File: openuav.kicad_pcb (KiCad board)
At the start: 4 copper layers, 36 x 36 mm, 72 parts, among them J1 Conn_01x01, J10 Conn_01x01, J11 Conn_01x01, J12 Conn_01x01, J13 Conn_01x01, J14 Conn_01x01, J15 Conn_01x01, J16 Conn_01x01, J17 Conn_ARM_SWD_TagConnect_TC203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, J19 Conn_01x01, J2 Conn_01x01, J20 Conn_01x01, J21 Conn_01x01, J22 Conn_01x01, J23 Conn_01x01, J24 Conn_01x01, J25 Conn_01x01, J26 Conn_01x01, J27 Conn_01x01, J28 Conn_01x01, J29 Conn_01x01, J3 Conn_01x01, J30 Conn_01x01, J31 Conn_01x01, J4 Conn_01x01, J5 Conn_01x01, J6 Conn_01x01, J7 Conn_01x01, J8 Conn_01x01, J9 Conn_01x01, J99 USB_C_Receptacle_USB2.0, Q2 AO3400A, SW1 SW_Push, U1 STM32G474CETx, U2 BMI270, U3 BMP280, U5 TPS54202DDC, U6 W25N01GVZEIG, U7 XC6206P332MR

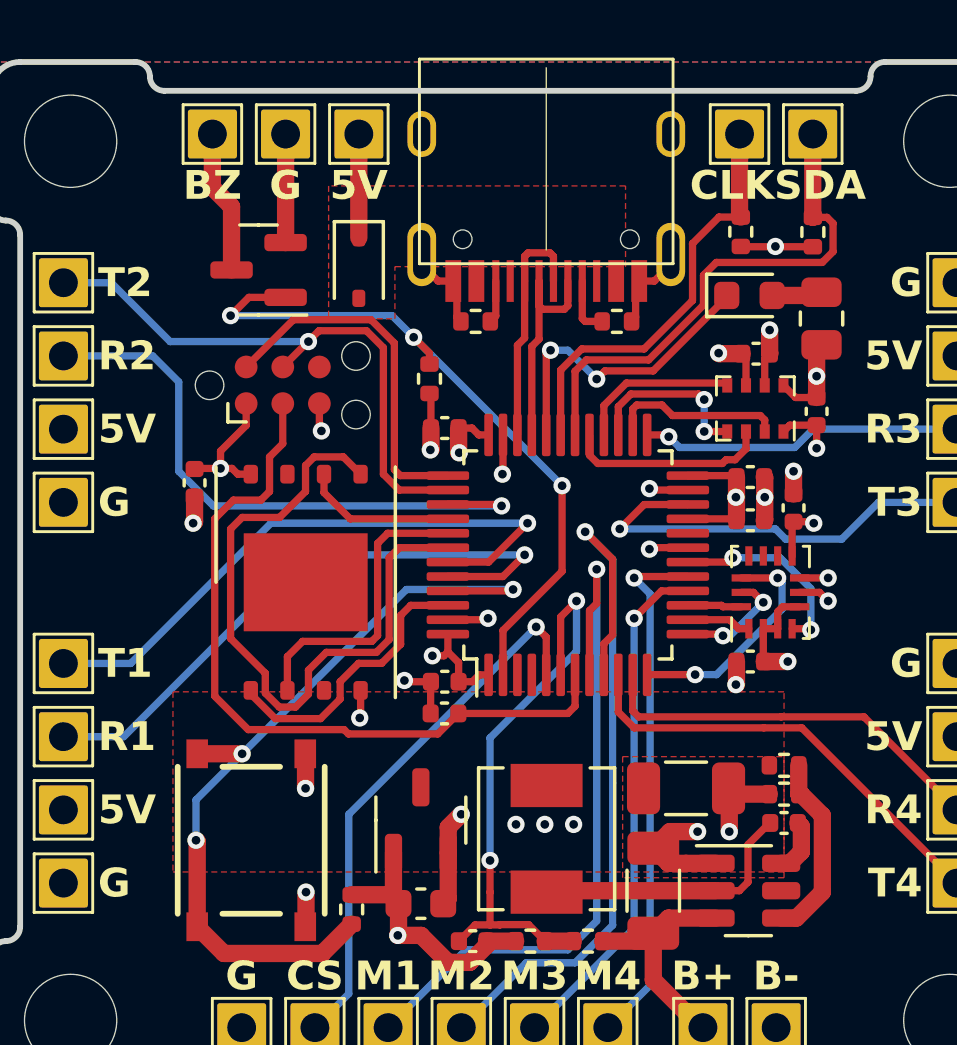
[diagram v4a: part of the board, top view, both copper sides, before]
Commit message: rearrange buzzer pins to keep +5v away from USB GND
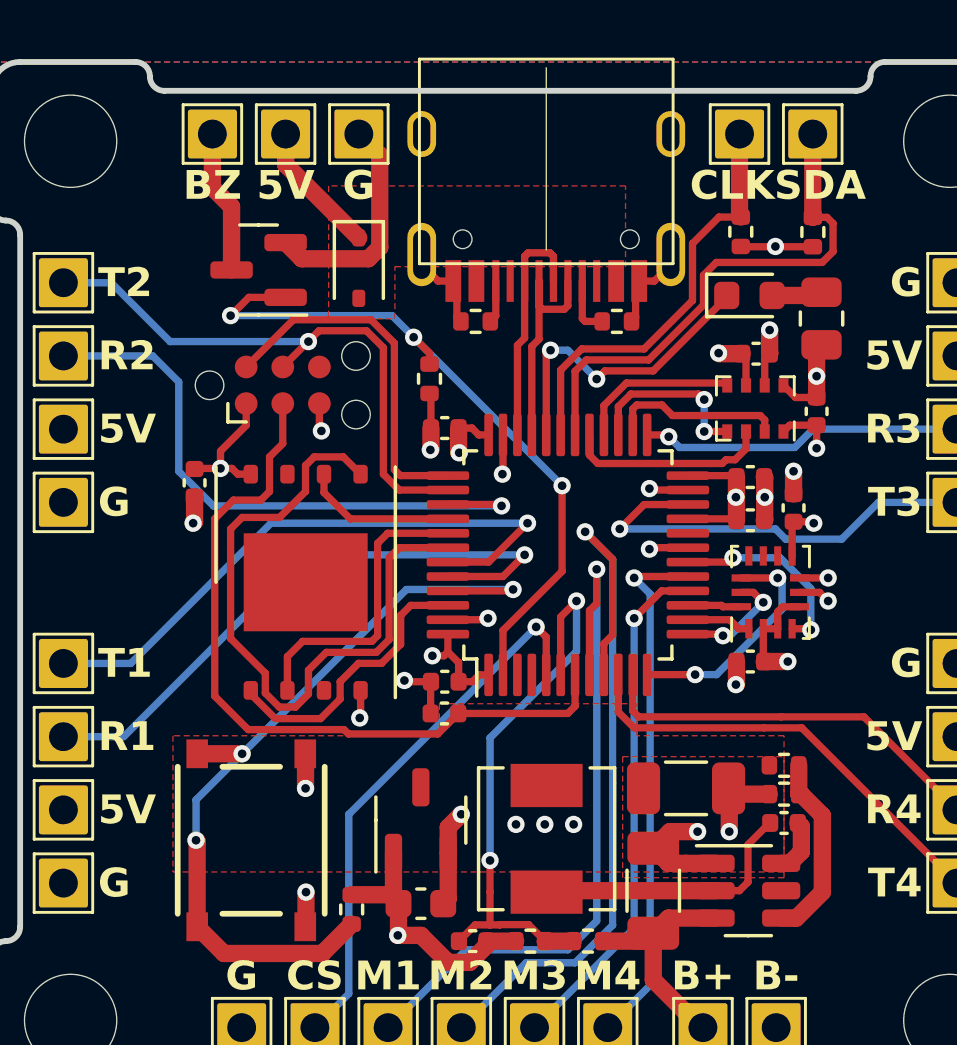
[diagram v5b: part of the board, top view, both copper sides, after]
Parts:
- moved J27 2.54 mm to (142.7, 52.5)
- moved J28 2.54 mm to (140.2, 52.5)
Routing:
- net GND: track 48.1 -> 52.3 mm
- net +5V: track 3.60 -> 4.65 mm
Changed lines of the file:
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@@
   )
   (footprint "Connector_Custom_Pads:TP-2.54" (layer "F.Cu")
-    (at 142.748 52.5 180)
+    (at 140.208 52.5 180)
     (property "Sheetfile" "openuav.kicad_sch")
     (property "Sheetname" "")
@@
   )
   (footprint "Connector_Custom_Pads:TP-2.54" (layer "F.Cu")
-    (at 140.208 52.5 180)
+    (at 142.748 52.5 180)
     (property "Sheetfile" "openuav.kicad_sch")
     (property "Sheetname" "")
@@
     (effects (font (size 1.5 1.5) (thickness 0.3) bold) (justify left bottom mirror))
   )
-  (gr_text "G" (at 140.208 53.7) (layer "F.SilkS")
+  (gr_text "G" (at 142.748 53.7) (layer "F.SilkS")
     (effects (font (size 1 1) (thickness 0.2) bold) (justify top))
   )
@@
     (effects (font (size 1 1) (thickness 0.2) bold) (justify bottom))
   )
-  (gr_text "5V" (at 142.748 53.7) (layer "F.SilkS")
+  (gr_text "5V" (at 140.208 53.7) (layer "F.SilkS")
     (effects (font (size 1 1) (thickness 0.2) bold) (justify top))
   )
@@
   (segment (start 146.594859 81.237) (end 147.18 80.651859) (width 0.6) (layer "F.Cu") (net 2))
   (segment (start 157 59.3) (end 157 60.11) (width 0.6) (layer "F.Cu") (net 2))
+  (segment (start 143.475 56.435968) (end 143.475 53.227) (width 0.6) (layer "F.Cu") (net 2))
   (segment (start 156.83 65.88) (end 156.81 65.9) (width 0.6) (layer "F.Cu") (net 2))
   (segment (start 152.35 57.6) (end 152.35 58.86) (width 0.254) (layer "F.Cu") (net 2))
   (segment (start 145.845142 81.237) (end 146.594859 81.237) (width 0.6) (layer "F.Cu") (net 2))
+  (segment (start 143.475 53.227) (end 142.748 52.5) (width 0.6) (layer "F.Cu") (net 2))
   (segment (start 144.93 57.03) (end 145.5 57.6) (width 0.254) (layer "F.Cu") (net 2))
   (segment (start 145.24 71.51) (end 145.25 71.5) (width 0.254) (layer "F.Cu") (net 2))
@@
   (segment (start 154.5 76.7) (end 153.5375 76.7) (width 0.6) (layer "F.Cu") (net 2))
   (segment (start 137.05 65.08) (end 137.05 65.95) (width 0.6) (layer "F.Cu") (net 2))
-  (segment (start 140.208 52.5) (end 140.208 56.266) (width 0.6) (layer "F.Cu") (net 2))
   (segment (start 146.15 57.6) (end 146.15 58.86) (width 0.254) (layer "F.Cu") (net 2))
   (segment (start 153.5375 76.7) (end 152.9625 77.275) (width 0.6) (layer "F.Cu") (net 2))
   (segment (start 145.24 72.6) (end 145.24 71.51) (width 0.254) (layer "F.Cu") (net 2))
+  (segment (start 143.083968 56.827) (end 143.475 56.435968) (width 0.6) (layer "F.Cu") (net 2))
   (segment (start 152.35 58.86) (end 152.21 59) (width 0.254) (layer "F.Cu") (net 2))
   (segment (start 156.83 64.42) (end 156.81 64.4) (width 0.6) (layer "F.Cu") (net 2))
@@
   (segment (start 154.1625 64.85) (end 152.88 64.85) (width 0.254) (layer "F.Cu") (net 2))
   (segment (start 137.05 65.95) (end 137 66) (width 0.6) (layer "F.Cu") (net 2))
+  (segment (start 140.208 56.266) (end 140.769 56.827) (width 0.6) (layer "F.Cu") (net 2))
   (segment (start 153.57 56.68) (end 153.57 57.03) (width 0.254) (layer "F.Cu") (net 2))
   (segment (start 158.63 62.6) (end 158.63 63.4) (width 0.254) (layer "F.Cu") (net 2))
   (segment (start 144.1 80.3) (end 144.908141 80.3) (width 0.6) (layer "F.Cu") (net 2))
   (segment (start 157 60.11) (end 157.01 60.12) (width 0.6) (layer "F.Cu") (net 2))
+  (segment (start 140.769 56.827) (end 143.083968 56.827) (width 0.6) (layer "F.Cu") (net 2))
   (segment (start 153.57 57.03) (end 153 57.6) (width 0.254) (layer "F.Cu") (net 2))
   (segment (start 158.73 68.4) (end 159.03 68.7) (width 0.254) (layer "F.Cu") (net 2))
@@
   (via (at 158.53 66) (size 0.6) (drill 0.3) (layers "F.Cu" "B.Cu") (net 4))
   (via (at 157.2 56.4) (size 0.6) (drill 0.3) (layers "F.Cu" "B.Cu") (net 4))
-  (segment (start 142.748 52.5) (end 142.748 56.1) (width 0.6) (layer "F.Cu") (net 5))
+  (segment (start 140.208 53.56) (end 142.748 56.1) (width 0.6) (layer "F.Cu") (net 5))
+  (segment (start 140.208 52.5) (end 140.208 53.56) (width 0.6) (layer "F.Cu") (net 5))
   (via (at 150.2 76.45) (size 0.6) (drill 0.3) (layers "F.Cu" "B.Cu") (free) (net 5))
   (via (at 149.2 76.45) (size 0.6) (drill 0.3) (layers "F.Cu" "B.Cu") (free) (net 5))
@@
     (polygon
       (pts
-        (xy 157.5 71.85)
-        (xy 136.3 71.85)
+        (xy 157.5 73.374)
+        (xy 152.4 73.374)
+        (xy 152.4 72.263)
+        (xy 145.542 72.263)
+        (xy 145.542 73.374)
+        (xy 136.3 73.374)
         (xy 136.3 78.1)
         (xy 157.5 78.1)
@@
   (zone (net 0) (net_name "") (layers "F&B.Cu") (hatch edge 0.5)
     (priority 1)
-    (connect_pads (clearance 0.3))
+    (connect_pads (clearance 0.25))
     (min_thickness 0.5) (filled_areas_thickness no)
     (fill yes (thermal_gap 0.5) (thermal_bridge_width 0.5) (island_removal_mode 1) (island_area_min 10))

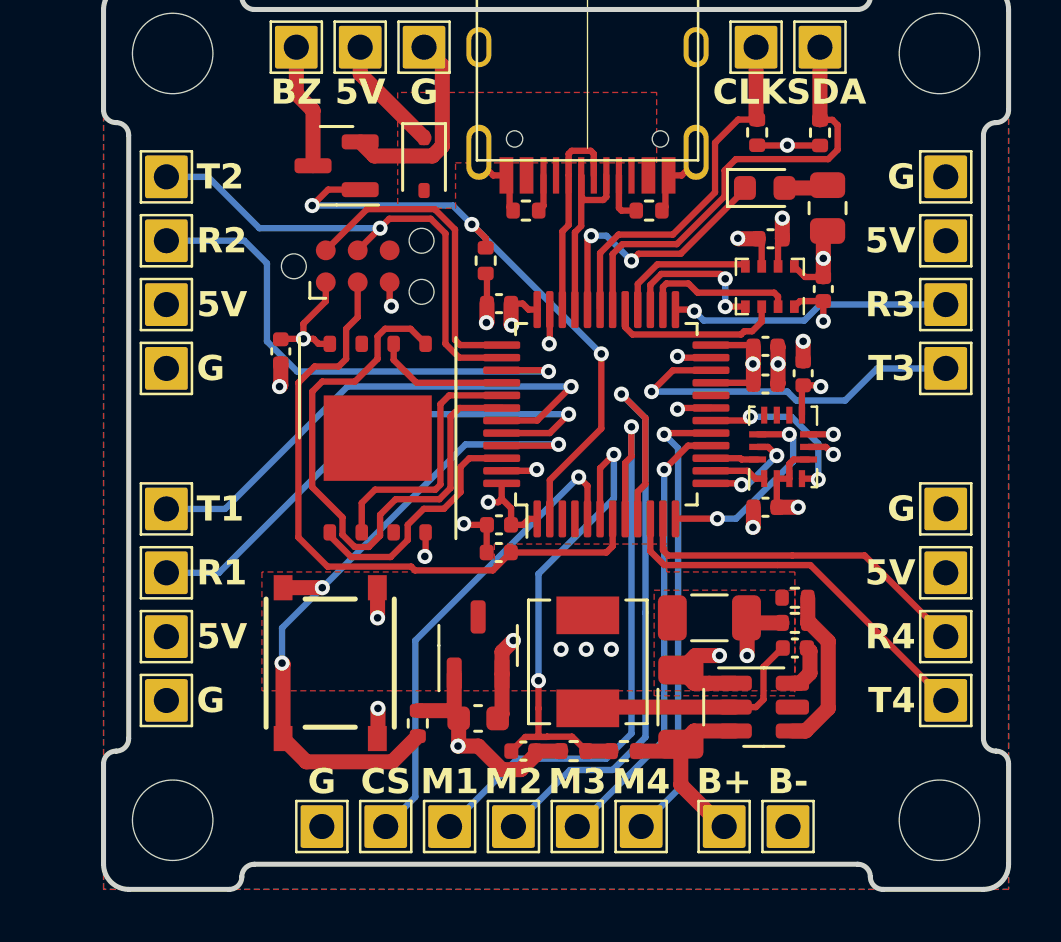
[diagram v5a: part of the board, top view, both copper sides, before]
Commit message: add vtx power switch, use smaller dfu button
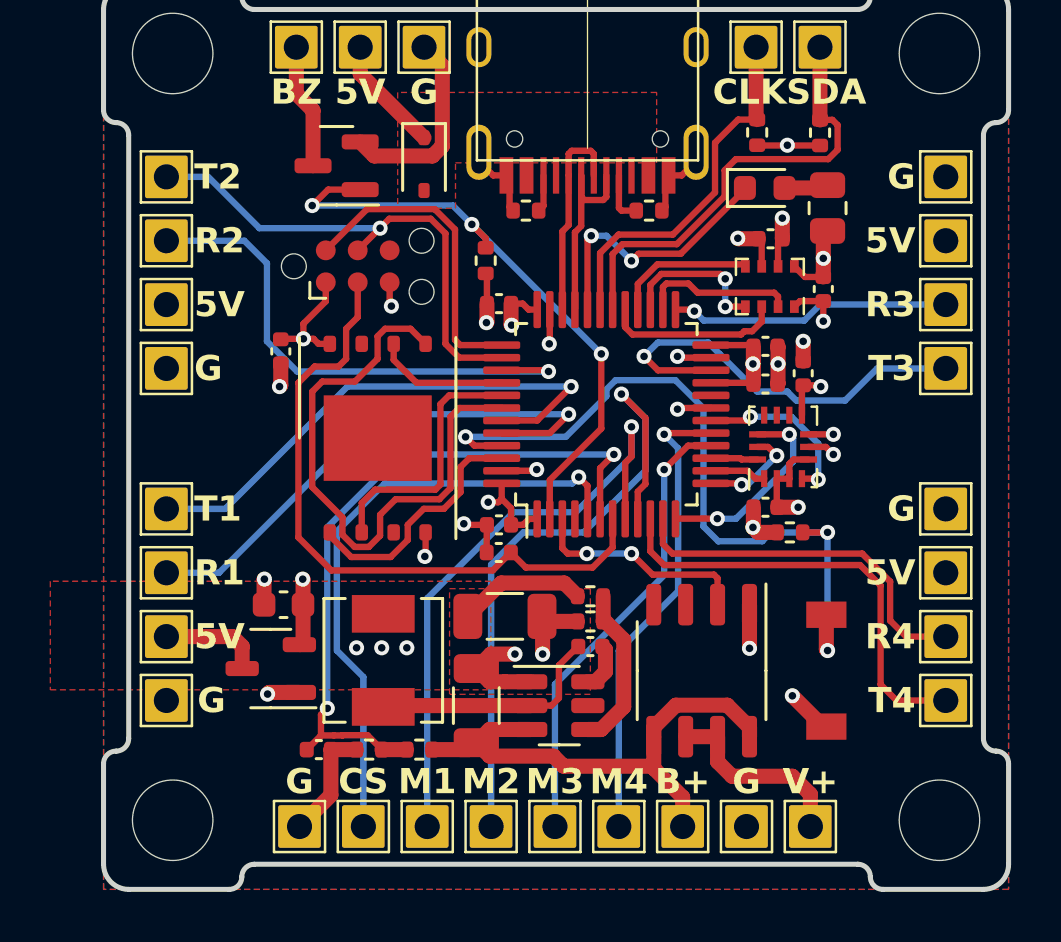
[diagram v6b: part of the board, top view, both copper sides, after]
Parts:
- added IC1: NCV8460A, Package_SO:SOP-8_3.9x4.9mm_P1.27mm, F.Cu at (153.8, 77.3)
- added J18: Conn_01x01, Connector_Custom_Pads:TP-2.54, F.Cu at (158.1, 83.5)
- SW1: footprint Connector_Custom_Pads:TS-1187A-B-A-B -> Connector_Custom_Pads:GT-TC029B-H025-L1N
- moved SW1 19.7 mm to (158.8, 77.3), turned to -90 degrees
- moved R8 16.6 mm to (157.3, 71.8), turned to 180 degrees
- moved C15 8.97 mm to (137.2, 74.7)
- moved U7 8.30 mm to (136.7, 77.2), turned to 180 degrees
- moved C10 8.14 mm to (149.4, 76.3)
- moved C14 8.14 mm to (138.6, 80.4)
- moved C2 8.14 mm to (146.0, 75.1)
- moved C9 8.14 mm to (144.8, 78.7)
- moved L1 8.14 mm to (141.1, 76.9)
- moved R3 8.14 mm to (149.4, 74.3)
- moved R4 8.14 mm to (149.4, 75.3)
- moved R5 8.14 mm to (142.6, 80.4)
- moved R6 8.14 mm to (140.6, 80.4)
- moved U5 8.14 mm to (148.1, 78.7)
- moved J30 1.65 mm to (153.0, 83.5)
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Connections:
- U1 pad 3: unconnected-(U1-PC14-Pad3) -> PSWITCH
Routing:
- net +BATT: track 7.89 -> 20.7 mm
- net +5V: track 4.65 -> 13.8 mm
- net PSWITCH: track 0.00 -> 8.89 mm, vias 0 -> 2
- net VOLTAGE: track 19.7 -> 28.2 mm
- net VPOWER: track 0.00 -> 7.78 mm
- net CURRENT: track 18.9 -> 24.5 mm
- net UART_4_TX: track 15.5 -> 17.8 mm
- net UART_3_TX: track 15.1 -> 16.6 mm
- net BOOT0: track 28.4 -> 29.8 mm
- net +3V3: track 34.4 -> 33.2 mm, vias 12 -> 11
- net PWM_2: track 26.2 -> 27.0 mm
- net UART_4_RX: track 13.9 -> 14.7 mm
- net NRST: track 26.2 -> 26.7 mm
- net GND: track 52.3 -> 52.4 mm, vias 19 -> 21
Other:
- board text added: "V+"
- board text removed: "B-"

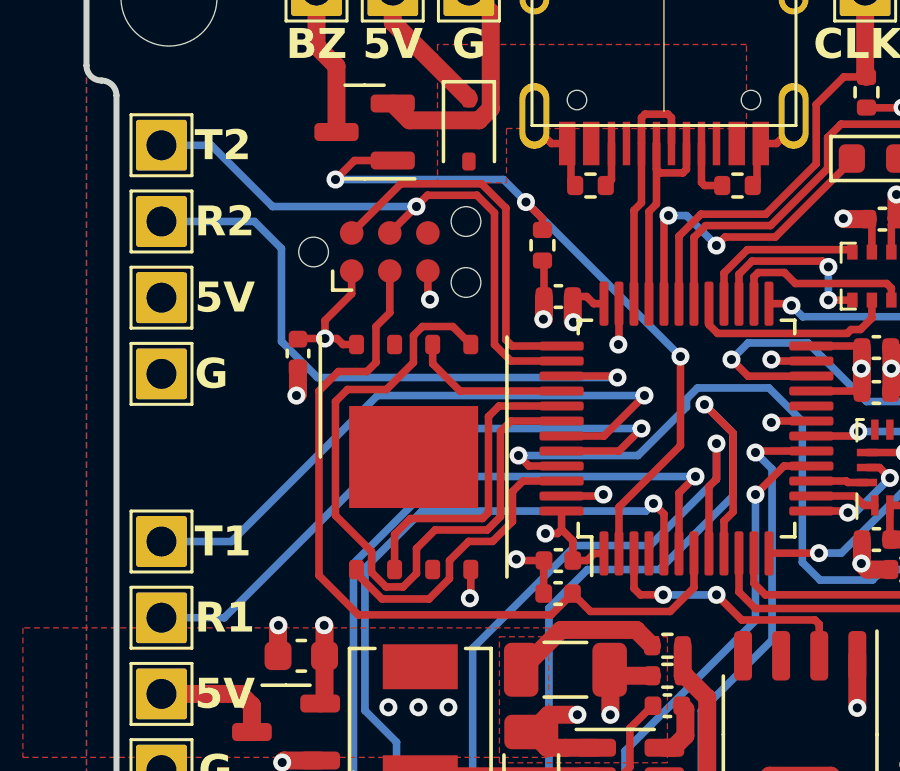
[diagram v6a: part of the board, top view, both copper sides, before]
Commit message: Add missing connections on flash HOLD and WP pins Make 5V plane slightly larger in corners to make space for tooling holes
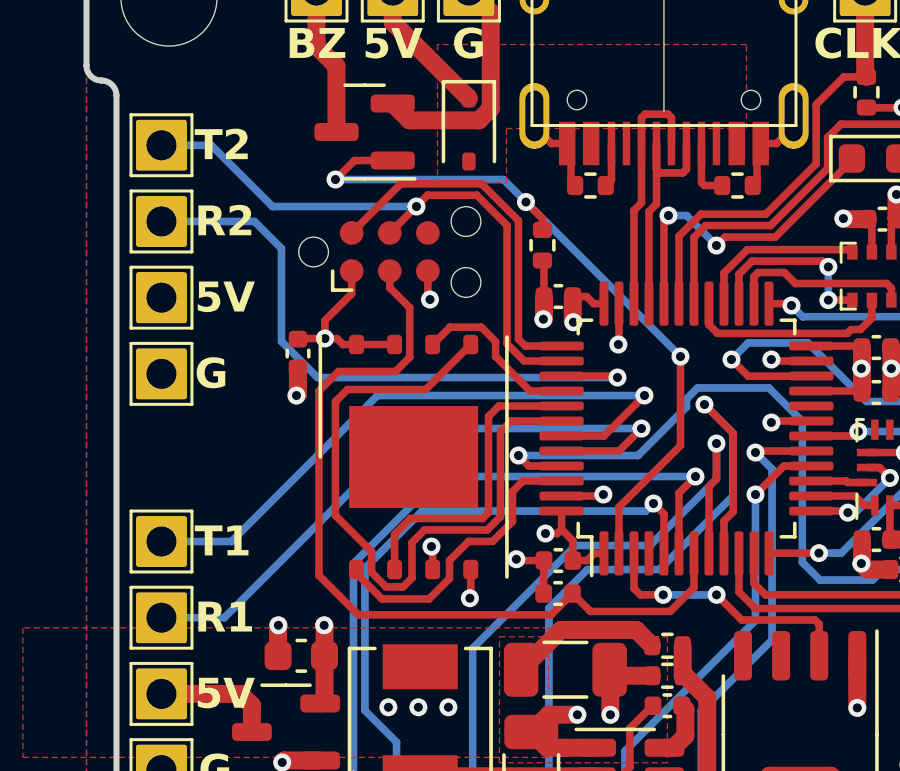
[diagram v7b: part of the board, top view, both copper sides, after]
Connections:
- U6 pad 3: unconnected-(U6-IO2-Pad3) -> +3V3
- U6 pad 7: unconnected-(U6-IO3-Pad7) -> +3V3
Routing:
- net +3V3: track 33.2 -> 35.3 mm, vias 11 -> 12
- net NRST: track 26.7 -> 27.8 mm
- net SPI3_MOSI: track 23.5 -> 22.7 mm

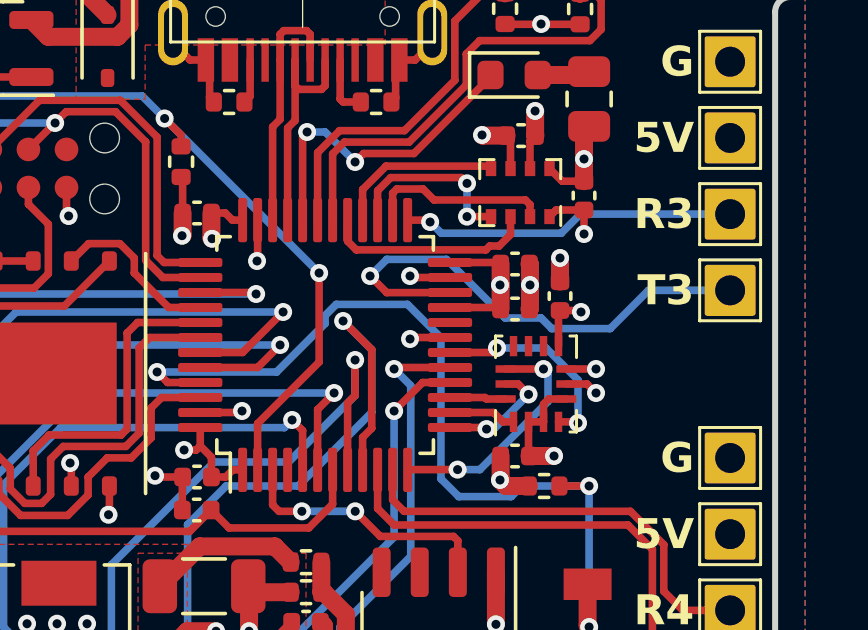
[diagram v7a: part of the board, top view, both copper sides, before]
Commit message: Connect VREF+ to 3v3
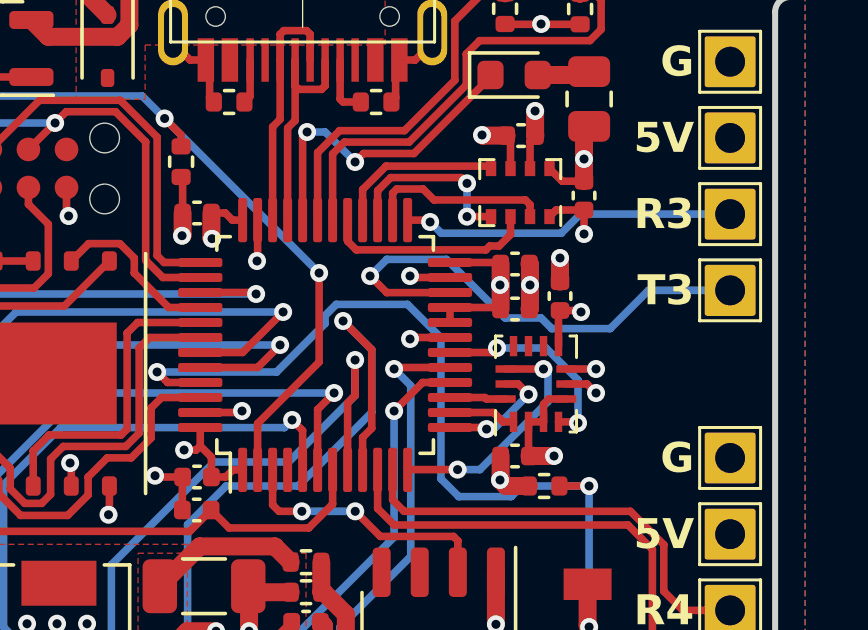
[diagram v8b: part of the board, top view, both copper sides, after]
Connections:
- U1 pad 20: unconnected-(U1-VREF+-Pad20) -> +3V3
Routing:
- net +3V3: track 35.3 -> 35.8 mm
